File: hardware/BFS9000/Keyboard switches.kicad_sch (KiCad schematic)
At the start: 117 parts

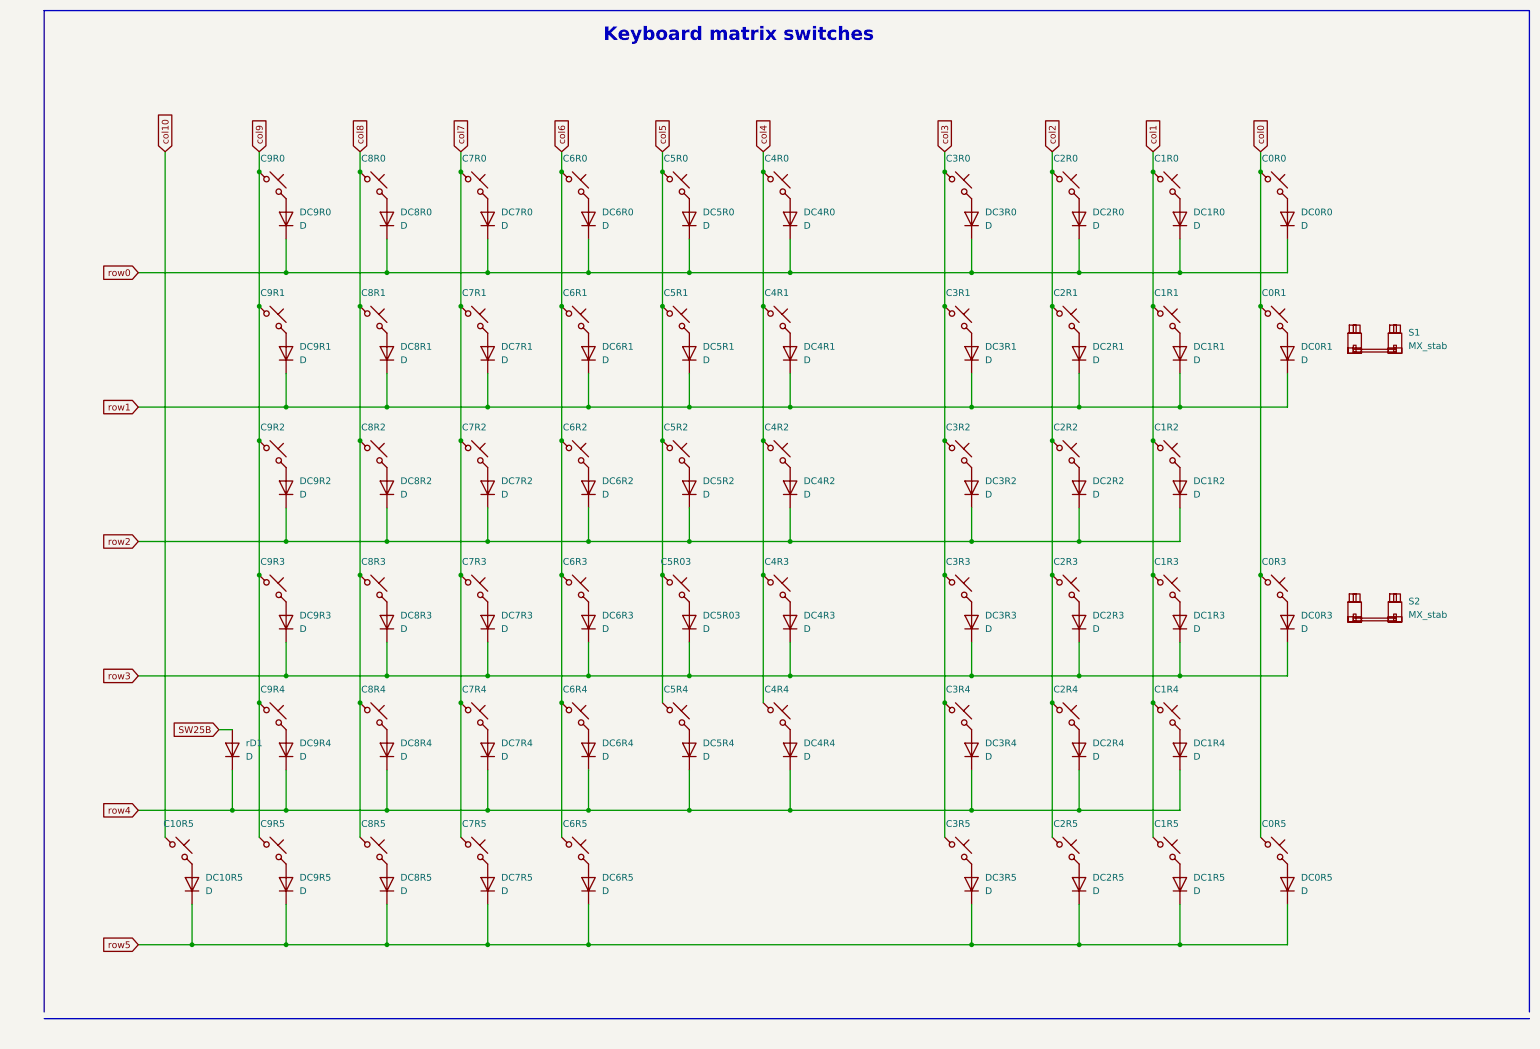
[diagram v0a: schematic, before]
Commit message: feat(hardware): update BFS9000 schematic and PCB layout
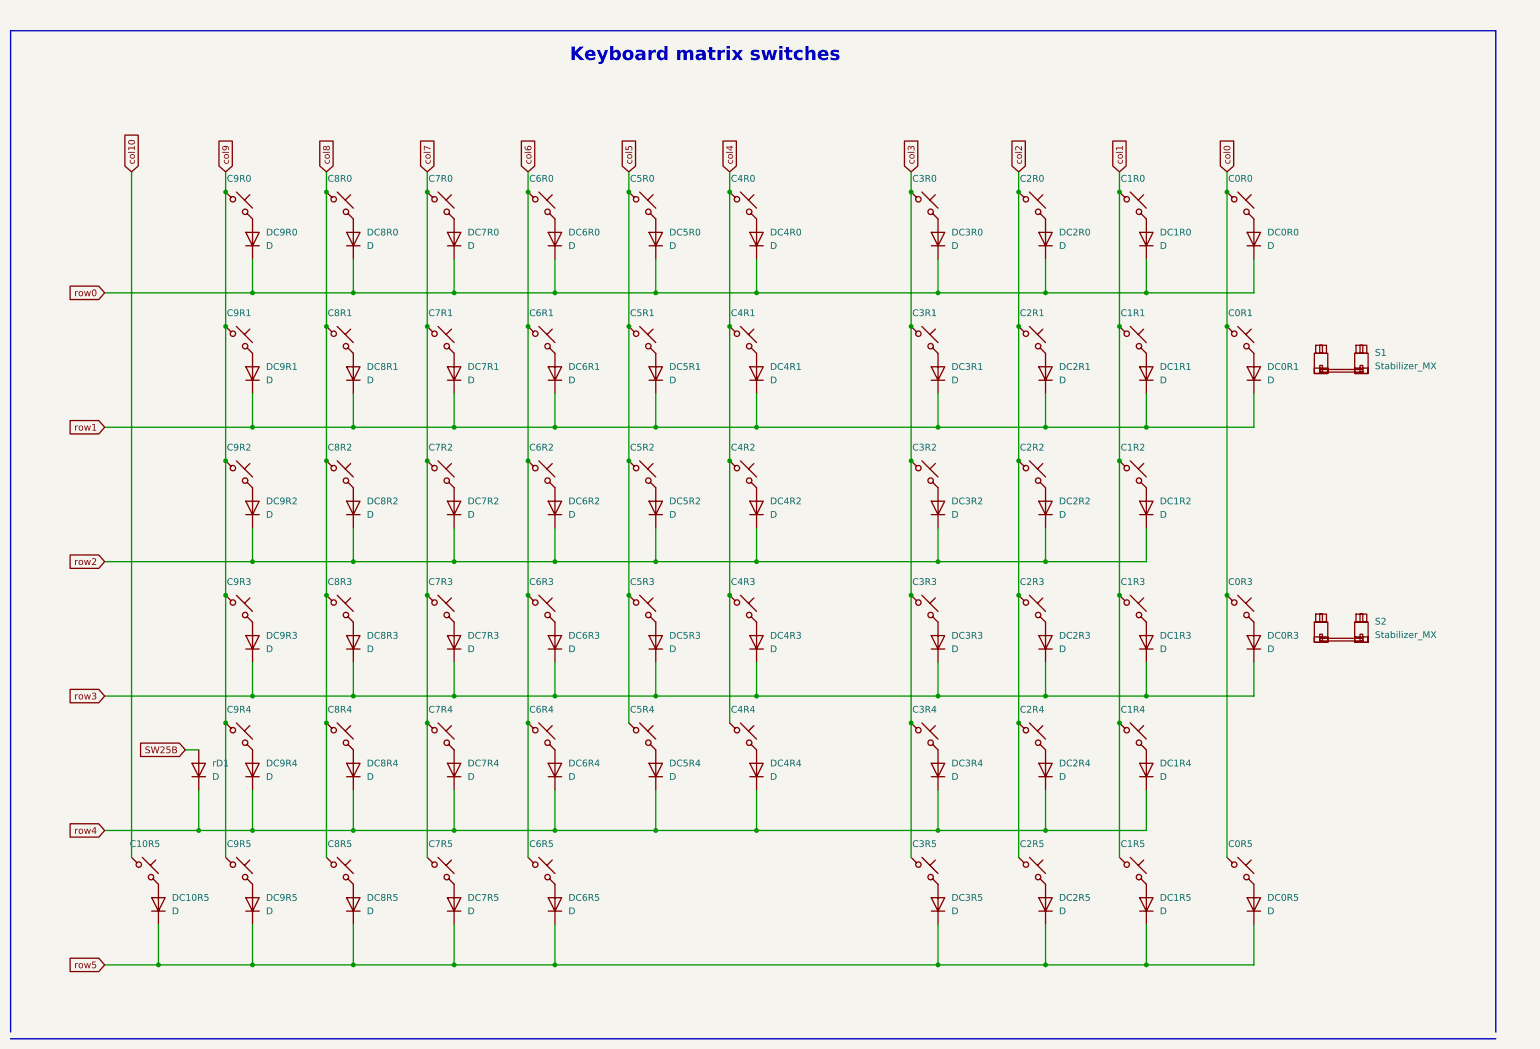
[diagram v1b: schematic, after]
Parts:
- C0R0, C0R1, C0R3, C0R5, C10R5, C1R0, C1R1, C1R2, C1R3, C1R4, C1R5, C2R0, C2R1, C2R2, C2R3, C2R4, C2R5, C3R0, C3R1, C3R2, C3R3, C3R4, C3R5, C4R0, C4R1, C4R2, C4R3, C4R4, C5R0, C5R1, C5R2, C5R4, C6R0, C6R1, C6R2, C6R3, C6R4, C6R5, C7R0, C7R1, C7R2, C7R3, C7R4, C7R5, C8R0, C8R1, C8R2, C8R3, C8R4, C8R5, C9R0, C9R1, C9R2, C9R3, C9R4, C9R5: footprint BFS9000:Cherry_MX_DS_Hotswap_Vertical -> BFS9000:SW_Cherry_MX_Hotswap_DS; symbol PCM_marbastlib-mx:MX_SW_HS_CPG151101S11 -> BFS9000:SW_MX_Hotswap
- C5R3: renamed from C5R03; footprint BFS9000:Cherry_MX_DS_Hotswap_Vertical -> BFS9000:SW_Cherry_MX_Hotswap_DS; symbol PCM_marbastlib-mx:MX_SW_HS_CPG151101S11 -> BFS9000:SW_MX_Hotswap
- DC0R0, DC0R1, DC0R3, DC0R5, DC10R5, DC1R0, DC1R1, DC1R2, DC1R3, DC1R4, DC1R5, DC2R0, DC2R1, DC2R2, DC2R3, DC2R4, DC2R5, DC3R0, DC3R1, DC3R2, DC3R3, DC3R4, DC3R5, DC4R0, DC4R1, DC4R2, DC4R3, DC4R4, DC5R0, DC5R1, DC5R2, DC5R4, DC6R0, DC6R1, DC6R2, DC6R3, DC6R4, DC6R5, DC7R0, DC7R1, DC7R2, DC7R3, DC7R4, DC7R5, DC8R0, DC8R1, DC8R2, DC8R3, DC8R4, DC8R5, DC9R0, DC9R1, DC9R2, DC9R3, DC9R4, DC9R5, rD1: footprint BFS9000:D_SOD-123_DO-35_Hybrid_DoubleSided_V2 -> BFS9000:D_Hybrid_SOD-123_DO-35_DS; symbol BFS9000:D-Lily58-cache-Lily58_Pro-rescue -> BFS9000:D
- DC5R3: renamed from DC5R03; footprint BFS9000:D_SOD-123_DO-35_Hybrid_DoubleSided_V2 -> BFS9000:D_Hybrid_SOD-123_DO-35_DS; symbol BFS9000:D-Lily58-cache-Lily58_Pro-rescue -> BFS9000:D
- S1, S2: value MX_stab -> Stabilizer_MX; footprint PCM_marbastlib-mx:STAB_MX_2u -> BFS9000:Stabilizer_MX_2u; symbol PCM_marbastlib-mx:MX_stab -> BFS9000:Stabilizer_MX
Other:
- moved on the sheet: C0R0, C0R1, C0R3, C0R5, C10R5, C1R0, C1R1, C1R2, C1R3, C1R4, C1R5, C2R0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
